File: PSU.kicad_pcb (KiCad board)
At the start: 4 copper layers, 100 x 100 mm, 182 parts, among them IC400 TLP185xSE, IC401 TLP185xSE, IC403 ACS71240, IC407 TLP185xSE, IC410 TLP185xSE, J200 09031967921, J400 XT60-Angled-F, J401 Conn_01x06_Pin, J800 USB_C_Receptacle_USB2.0_16P, Q400 AO3400A, Q401 HSBA8119, Q402 HSBA8119, Q403 HSBA8119, Q404 AO3400A, Q700 MMST3904, SW400 TL2243, SW401 Push SW, U100 W25Q128, U301 TPS563201DDCR, U302 CH334P, U400 STM32H750VBTx, U401 TPD2E2U06DCK, U402 TPD2E2U06DCK, U403 INA219AIDCNR, U404 ADS1115IDGS, U500 TJA1044GTK_3Z, U600 TJA1044GTK_3Z, U700 STM32F103CBTx, U801 FSUSB42UMX, X300 Q13FC1350000400, X400 X322512MSB4SI, Y700 8 MHz, Y900 12Mhz

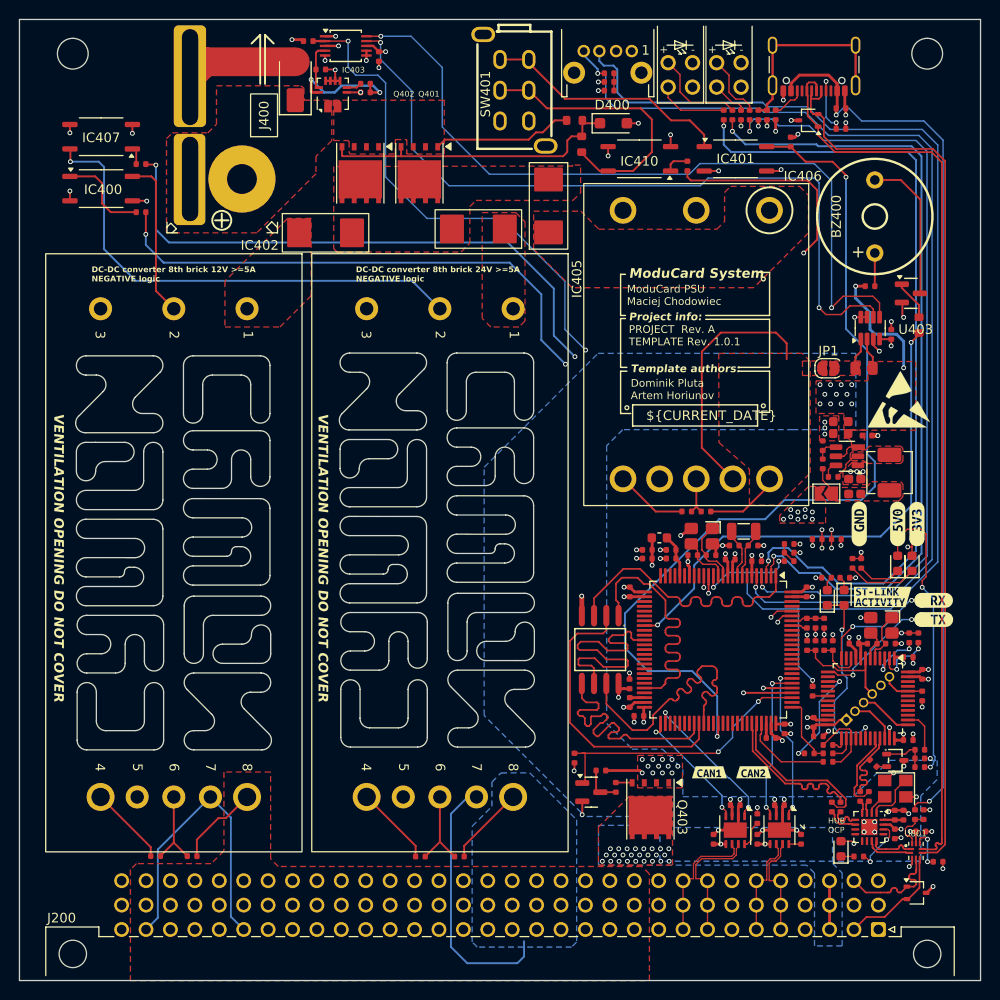
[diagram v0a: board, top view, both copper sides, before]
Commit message: Change MCU to STM32H563
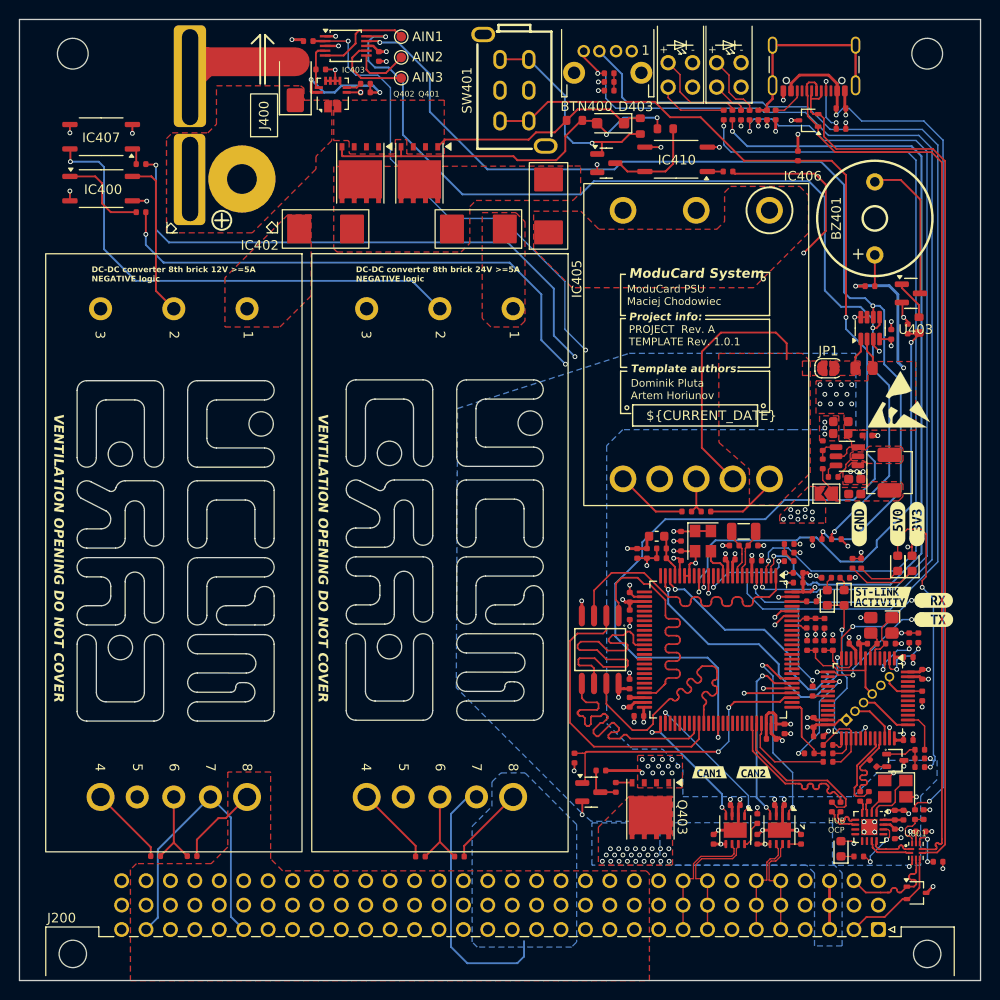
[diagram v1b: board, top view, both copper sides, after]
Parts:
- removed BZ400: Buzzer, BUZ-BD12:BUZ-TH_BD12.0-P7.60-D0.6-FD
- removed C407, C409, C415, C416: 100nF, PCM_JLCPCB:C_0402
- removed C408: 10uF, PCM_JLCPCB:C_0402
- removed C411, C412: 22pF, PCM_JLCPCB:C_0402
- removed C413, C414: 2.2uF, PCM_JLCPCB:C_0402
- removed D400: 20V, Diode_SMD:D_SOD-123F
- removed FB400: ~, PCM_JLCPCB:FB_0603
- removed IC401: TLP185xSE, Package_SO:SOIC-4_4.55x3.7mm_P2.54mm
- removed R404, R406: 100Ω, PCM_JLCPCB:R_0402
- removed R405, R431: 10kΩ, PCM_JLCPCB:R_0402
- removed R407: 1kΩ, PCM_JLCPCB:R_0402
- removed R408: 470Ω, PCM_JLCPCB:R_0402
- removed R409, R433: 120Ω, PCM_JLCPCB:R_0402
- removed R432: 3.3kΩ, PCM_JLCPCB:R_0603
- removed SW400: TL2243, TL2243:TL2243
- removed U400: STM32H750VBTx, Package_QFP:LQFP-100_14x14mm_P0.5mm
- removed X400: X322512MSB4SI, PCM_JLCPCB:CRYSTAL-SMD_4P-L3.2-W2.5-BL
- added BTN400: TL2243, TL2243:TL2243, F.Cu at (100.6, 56.8)
- added BZ401: Buzzer, BUZ-BD12:BUZ-TH_BD12.0-P7.60-D0.6-FD, F.Cu at (128.4, 72.0)
- added C417: 100nF, PCM_JLCPCB:C_0402, F.Cu at (100.7, 57.8)
- added C419: 100nF, PCM_JLCPCB:C_0402, F.Cu at (119.5, 105.9)
- added C420: 100nF, PCM_JLCPCB:C_0402, F.Cu at (116.1, 107.6)
- added C421: 100nF, PCM_JLCPCB:C_0402, F.Cu at (117.6, 126.1)
- added C422: 100nF, PCM_JLCPCB:C_0402, F.Cu at (120.4, 108.9)
- added C423: 10uF, PCM_JLCPCB:C_0402, F.Cu at (106.2, 106.3)
- added C424: 100nF, PCM_JLCPCB:C_0402, F.Cu at (106.2, 107.3)
- added C425: 10uF, PCM_JLCPCB:C_0402, F.Cu at (103.6, 106.8)
- added C426: 100nF, PCM_JLCPCB:C_0402, F.Cu at (104.7, 106.8)
- added C427: 2.2uF, PCM_JLCPCB:C_0402, F.Cu at (102.9, 122.3)
- added C429: 2.2uF, PCM_JLCPCB:C_0402, F.Cu at (121.8, 111.8)
- added C432: 100nF, PCM_JLCPCB:C_0402, F.Cu at (108.2, 105.1)
- added D403: 20V, Diode_SMD:D_SOD-123F, F.Cu at (100.9, 62.1)
- added FB401: ~, PCM_JLCPCB:FB_0603, F.Cu at (105.7, 105.1)
- added Q405: MMBT5551, PCM_JLCPCB:Q_SOT-23, F.Cu at (100.4, 66.2)
- added R434: 10kΩ, PCM_JLCPCB:R_0402, F.Cu at (100.7, 58.7)
- added R435: 10kΩ, PCM_JLCPCB:R_0402, F.Cu at (119.5, 106.8)
- added R436: 100Ω, PCM_JLCPCB:R_0402, F.Cu at (119.5, 107.6)
- added R437: 1kΩ, PCM_JLCPCB:R_0402, F.Cu at (121.3, 114.1)
- added R438: 100Ω, PCM_JLCPCB:R_0402, F.Cu at (100.7, 56.9)
- added R439: 10kΩ, PCM_JLCPCB:R_0402, F.Cu at (122.2, 114.1)
- added R440: 220Ω, PCM_JLCPCB:R_0402, F.Cu at (114.5, 61.2)
- added R441: 220Ω, PCM_JLCPCB:R_0402, F.Cu at (115.3, 61.2)
- added R442: 220Ω, PCM_JLCPCB:R_0402, F.Cu at (113.5, 61.2)
- added R443: 220Ω, PCM_JLCPCB:R_0402, F.Cu at (112.7, 61.2)
- added R445: 120Ω, PCM_JLCPCB:R_0402, F.Cu at (127.9, 79.0)
- added TP400: TestPoint, TestPoint:TestPoint_Pad_D1.0mm, F.Cu at (79.1, 53.1)
- added TP401: TestPoint, TestPoint:TestPoint_Pad_D1.0mm, F.Cu at (79.1, 55.2)
- added TP402: TestPoint, TestPoint:TestPoint_Pad_D1.0mm, F.Cu at (79.1, 57.4)
- added U405: STM32H562VGTx, Package_QFP:LQFP-100_14x14mm_P0.5mm, F.Cu at (112.1, 116.8)
- added Y400: ASE-xxxMHz, Oscillator:Oscillator_SMD_Abracon_ASE-4Pin_3.2x2.5mm, F.Cu at (110.5, 105.6)
- C403: value 100nF -> 10uF
- C406: value 10uF -> 100nF
- R400: value 1kΩ -> 15kΩ; footprint PCM_JLCPCB:R_0402 -> PCM_JLCPCB:R_0603
- R401: value 1kΩ -> 10kΩ
- R403: value 10kΩ -> 100kΩ; footprint PCM_JLCPCB:R_0402 -> PCM_JLCPCB:R_0603
- R415: value 1kΩ -> 5.1kΩ
- R711: value 33kΩ -> 39kΩ
- SW401: value Push SW -> ~
- moved R401 48.6 mm to (120.4, 65.5)
- moved R403 47.0 mm to (104.0, 62.4), turned to -90 degrees
- moved R402 32.1 mm to (131.8, 83.5), turned to 90 degrees
- moved C400 14.3 mm to (102.9, 113.2), turned to -90 degrees
- moved R400 7.13 mm to (106.6, 62.7), turned to 0 degrees
- moved R417 4.26 mm to (113.1, 67.1), turned to 0 degrees
- moved IC410 3.83 mm to (107.7, 65.8)
- moved C405 1.31 mm to (120.4, 109.9), turned to 180 degrees
- moved C406 1.20 mm to (108.2, 107.1), turned to 90 degrees
- moved C402 0.56 mm to (102.9, 111.4)
- moved F402 0.40 mm to (71.2, 73.1)
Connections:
- net /ST-LINK/STLINK_RX renamed /MCU/STLINK.RX
- net /ST-LINK/STLINK_TX renamed /MCU/STLINK.TX
- C406 pad 1: /MCU/+VDDA -> +3V3
- IC403 pad 2: Net-(IC403-IP–) -> Net-(D403-K)
- IC410 pad 6: Net-(IC410-Pad6) -> Net-(Q405-C)
- Q401 pad 1: Net-(IC403-IP–) -> Net-(D403-K)
- Q401 pad 2: Net-(IC403-IP–) -> Net-(D403-K)
- Q401 pad 3: Net-(IC403-IP–) -> Net-(D403-K)
- Q401 pad 4: Net-(D400-K) -> Net-(D403-A)
- Q402 pad 1: Net-(IC403-IP–) -> Net-(D403-K)
- Q402 pad 2: Net-(IC403-IP–) -> Net-(D403-K)
- Q402 pad 3: Net-(IC403-IP–) -> Net-(D403-K)
- Q402 pad 4: Net-(D400-K) -> Net-(D403-A)
- R400 pad 1: /MCU/USER_LED_1 -> Net-(D403-A)
- R400 pad 2: Net-(LED300-Pad1) -> Net-(Q405-C)
- R401 pad 1: /MCU/BOOT_EN -> /MCU/Power_Button_IN
- R401 pad 2: /MCU/BOOT0 -> +3V3
- R402 pad 1: /MCU/BOOT0 -> /MCU/Buzzer
- R403 pad 1: +3V3 -> Net-(D403-K)
- R403 pad 2: /MCU/NRST -> Net-(Q405-B)
- R415 pad 1: Net-(IC403-IP–) -> Net-(D403-K)
- R415 pad 2: Net-(D400-K) -> Net-(D403-A)
- SW401 pad 1: GND -> /MCU/Power_Button_IN
- SW401 pad 2: Net-(IC410-Pad6) -> GND
- SW401 pad 3: Net-(IC401-Pad1) -> Net-(Q405-B)
- SW401 pad 4: GND -> /MCU/Power_Button_IN
- SW401 pad 5: Net-(IC410-Pad6) -> GND
- SW401 pad 6: Net-(IC401-Pad1) -> Net-(Q405-B)
- U404 pad 10: /Battery connector/ADS1115.SCL -> /5V converter + sensor/I2C.SCL
- U404 pad 5: GND -> Net-(U404-AIN1)
- U404 pad 6: GND -> Net-(U404-AIN2)
- U404 pad 7: GND -> Net-(U404-AIN3)
- U404 pad 9: /Battery connector/ADS1115.SDA -> /5V converter + sensor/I2C.SDA
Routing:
- net Net-(D403-A): track 0.00 -> 40.1 mm, vias 0 -> 2
- net /MCU/Power_Button_IN: track 95.5 -> 131.4 mm
- net Net-(D400-K): track 32.1 -> 0.00 mm
- net Net-(IC410-Pad6): track 29.3 -> 0.00 mm
- net /MCU/STLINK.TX: track 12.1 -> 40.6 mm, vias 2 -> 4
- net Net-(IC401-Pad1): track 26.2 -> 0.00 mm
- net /MCU/STLINK.RX: track 12.7 -> 38.6 mm, vias 2 -> 4
- net Net-(D403-K): track 0.00 -> 23.5 mm
- net Net-(Q405-B): track 0.00 -> 22.7 mm, vias 0 -> 1
- net +3V3: track 63.5 -> 79.2 mm, vias 41 -> 44
- net Net-(IC403-IP–): track 14.6 -> 0.00 mm
- net Net-(U404-AIN1): track 0.00 -> 9.87 mm
- net Net-(Q405-C): track 0.00 -> 9.77 mm
- net Net-(U404-AIN3): track 0.00 -> 8.46 mm
- net /5V converter + sensor/I2C.SCL: track 118.3 -> 126.6 mm, vias 5 -> 4
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- added copper zone on F.Cu, net Net-(D403-K)
- removed copper zone on F.Cu, net Net-(IC403-IP–)
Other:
- outline, holes or cut-outs redrawn
- board text added: "AIN1"
- board text added: "AIN2"
- board text added: "AIN3"

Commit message: Add LCSC numbers
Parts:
- removed R711: 39kΩ, PCM_JLCPCB:R_0402
- added R404: 36kΩ, PCM_JLCPCB:R_0603, F.Cu at (133.4, 128.0)
- moved R710 0.82 mm to (133.8, 126.9)
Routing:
- net Net-(Q700-B): track 4.94 -> 5.82 mm
- net GND: track 148.0 -> 147.4 mm

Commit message: layout done
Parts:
- added ?: , , F.Cu at (44.9, 141.6)
- added ?: , , F.Cu at (46.5, 58.4)
- added REF**: ToolingHole_1.152mm, MountingHole:ToolingHole_1.152mm, F.Cu at (131.4, 58.1)
- added REF**: Part_Num_JLCPCB, PCM_JLCPCB:Part_Num_JLCPCB, F.Cu at (122.0, 83.2)
